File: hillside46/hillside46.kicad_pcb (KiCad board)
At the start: 2 copper layers, 142.5 x 99.9 mm, 80 parts, among them J1 Haptic, J2 TRRS, J3 Bat_Pos, J4 Bat_Neg, J5 Bat_Pos, J6 Bat_Neg, K1 SW_Key, K10 SW_Key, K11 SW_Key, K12 SW_Key, K13 SW_Key, K14 SW_Key, K15 SW_Key, K16 SW_Key, K17 SW_Key, K18 SW_Key, K19 SW_Rotary, K2 SW_Key, K23 SW_Rotary, K24 SW_Key, K25 SW_Key, K26 SW_Key, K3 SW_Key, K4 SW_Key, K5 SW_Key, K6 SW_Key, K7 SW_Key, K8 SW_Key, K9 SW_Key, SW1 Reset, SW2 SW_Power, U1 ProMicro_r

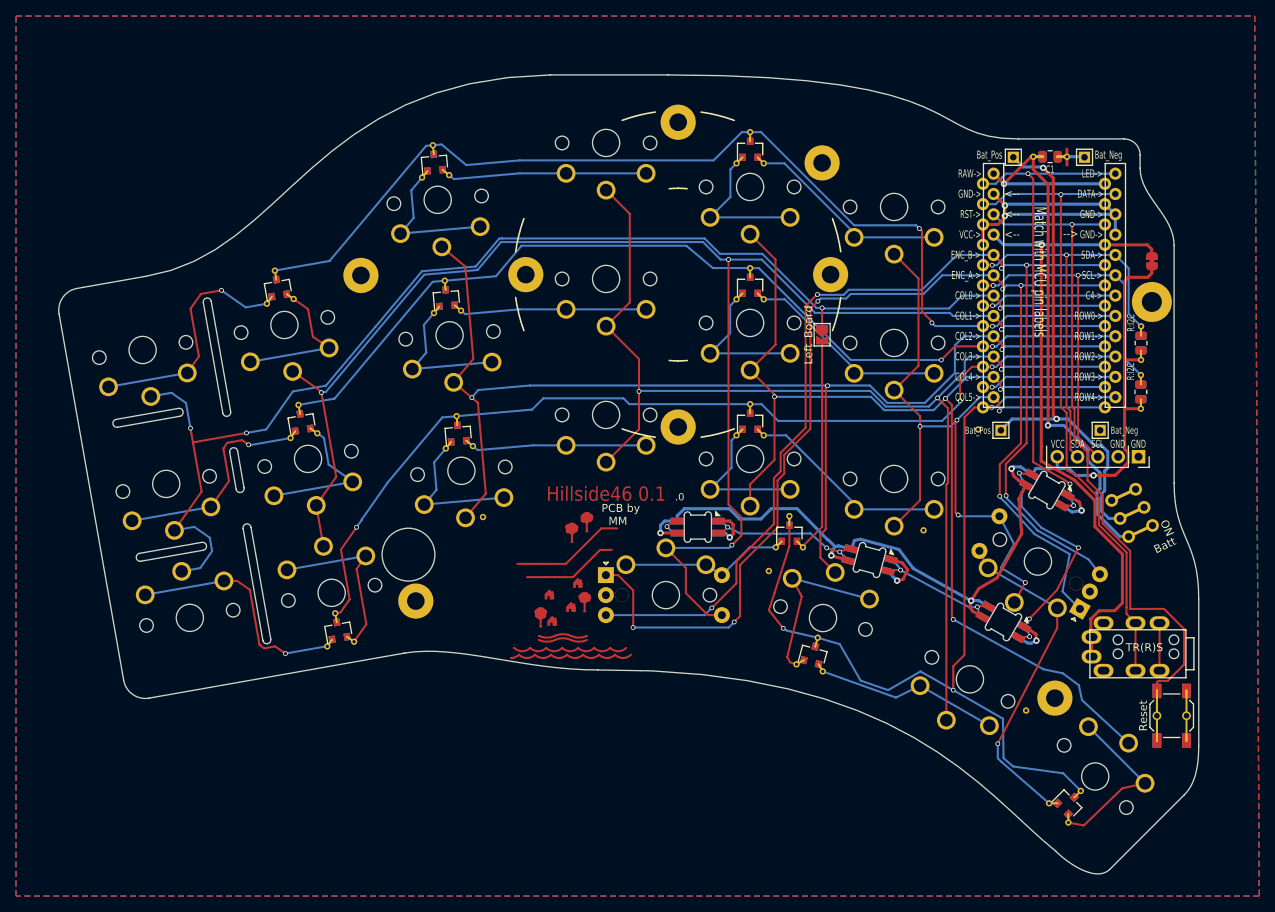
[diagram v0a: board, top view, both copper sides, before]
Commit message: 46: Fix bump-on spots and cutout callouts
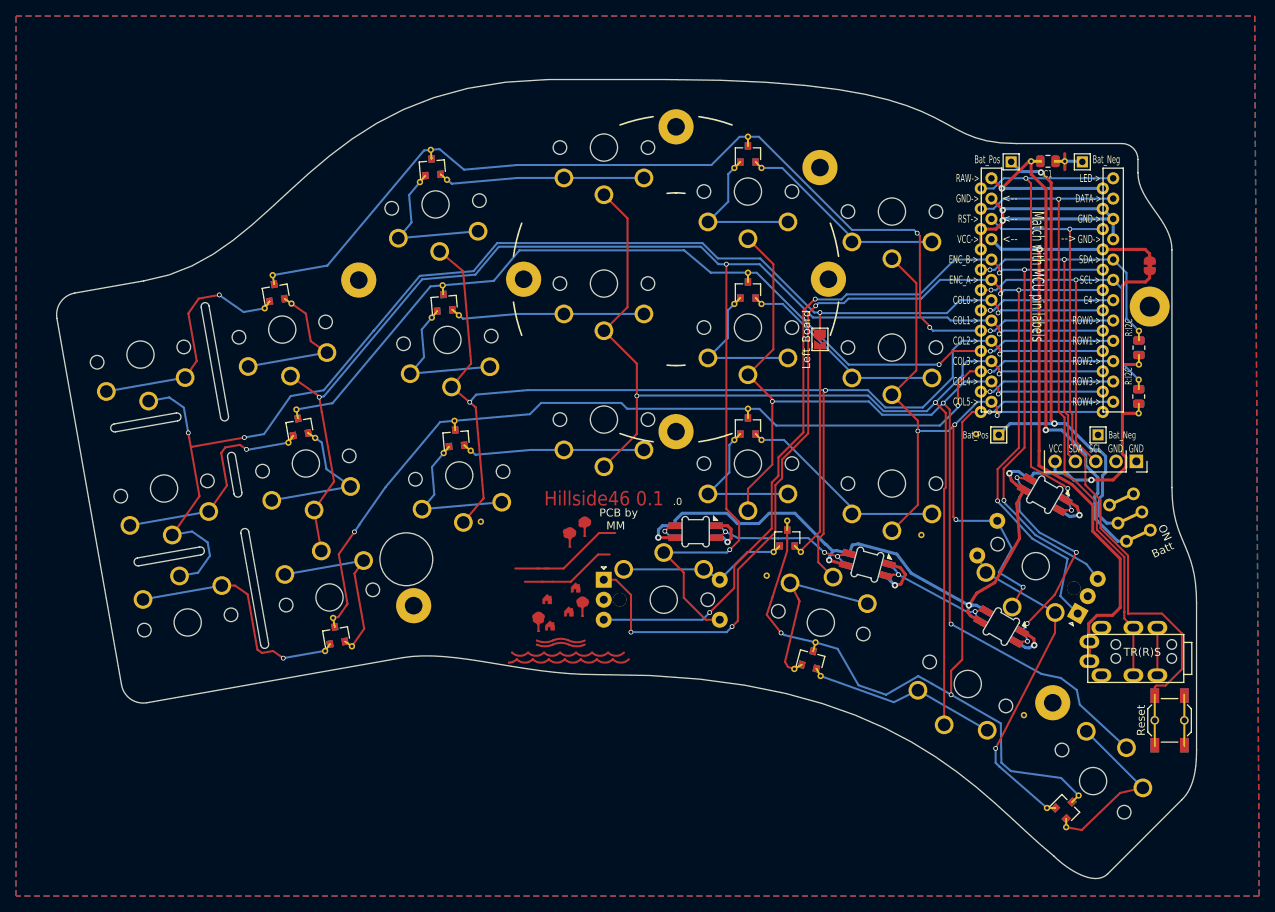
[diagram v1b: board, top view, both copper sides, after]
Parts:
- moved H17 119.6 mm to (185.2, 61.4), turned to 0 degrees
- moved H8 22.8 mm to (170.5, 124.4)
- moved H11 16.5 mm to (133.7, 120.5)
- moved H2 15.8 mm to (105.6, 123.3)
- moved H13 2.65 mm to (88.7, 99.5)
- moved H12 1.21 mm to (93.3, 126.0)
- moved D15 0.64 mm to (166.0, 96.0)
- moved H19 0.64 mm to (200.5, 137.1)
- moved K26 0.64 mm to (209.2, 140.4)
- moved C1 0.64 mm to (203.5, 62.9)
- moved D19 0.64 mm to (170.9, 110.0)
- moved D3 0.64 mm to (180.9, 113.3)
- moved D4 0.64 mm to (159.5, 109.2)
- moved D8 0.64 mm to (126.6, 63.6)
- moved H21 0.64 mm to (203.8, 68.8)
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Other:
- board text added: "CUT"

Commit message: 46: Cleanup edge, logo, row numbers
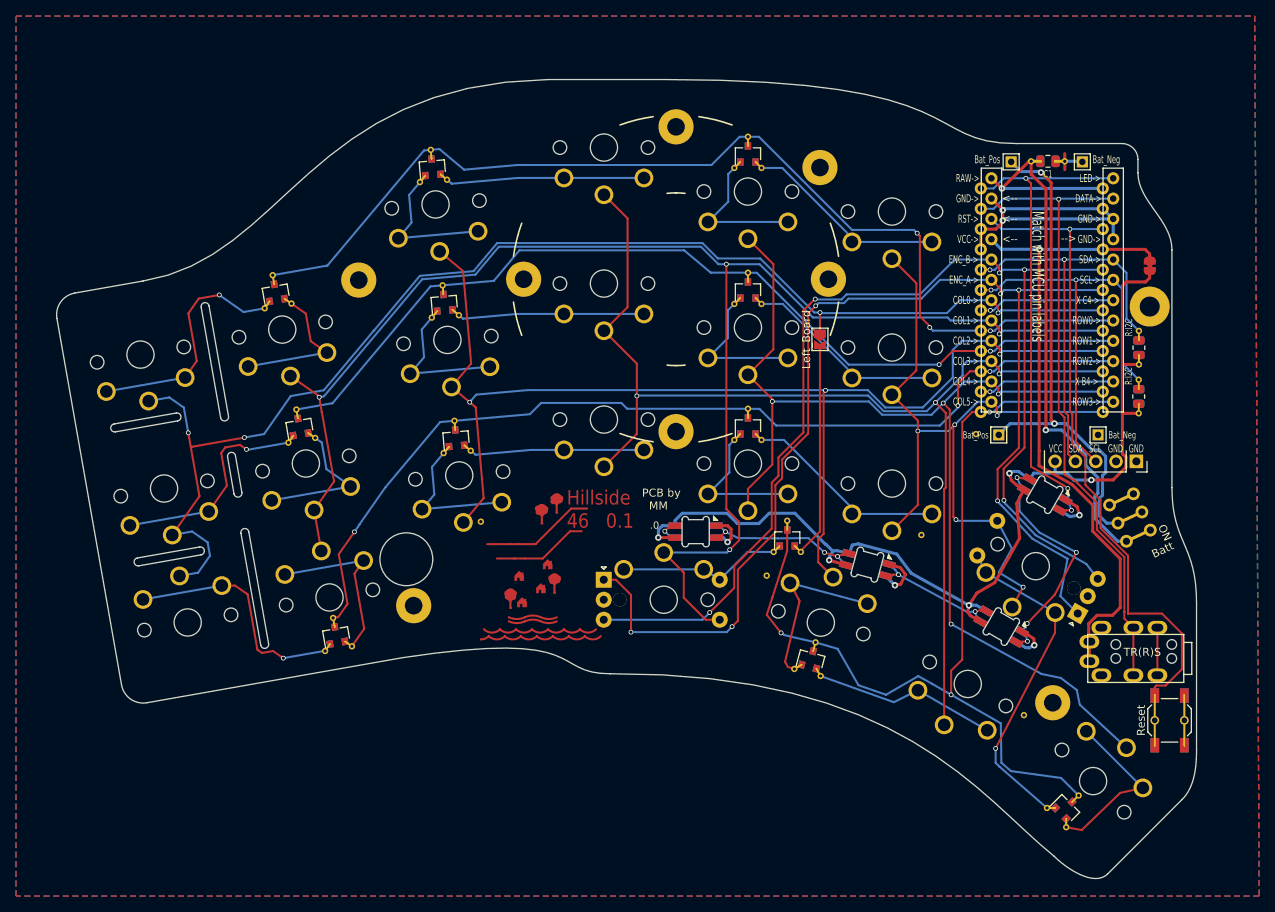
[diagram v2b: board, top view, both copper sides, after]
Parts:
- moved H3 4.55 mm to (139.6, 114.1)
- moved H11 2.55 mm to (135.6, 118.8)
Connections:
- net row4 renamed row3
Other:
- outline, holes or cut-outs redrawn
- board text added: "Hillside 46 0.1"
- board text removed: "Hillside46 0.1"

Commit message: 46: PCBA
- BOM JLC part numbers, type, and cost
- ESD protection chip
- PCBA Tooling holes
- Resistor values
- Reset switch model
- BOM excludes switches, vias, etch
- Paste layers
- JLC order number silk
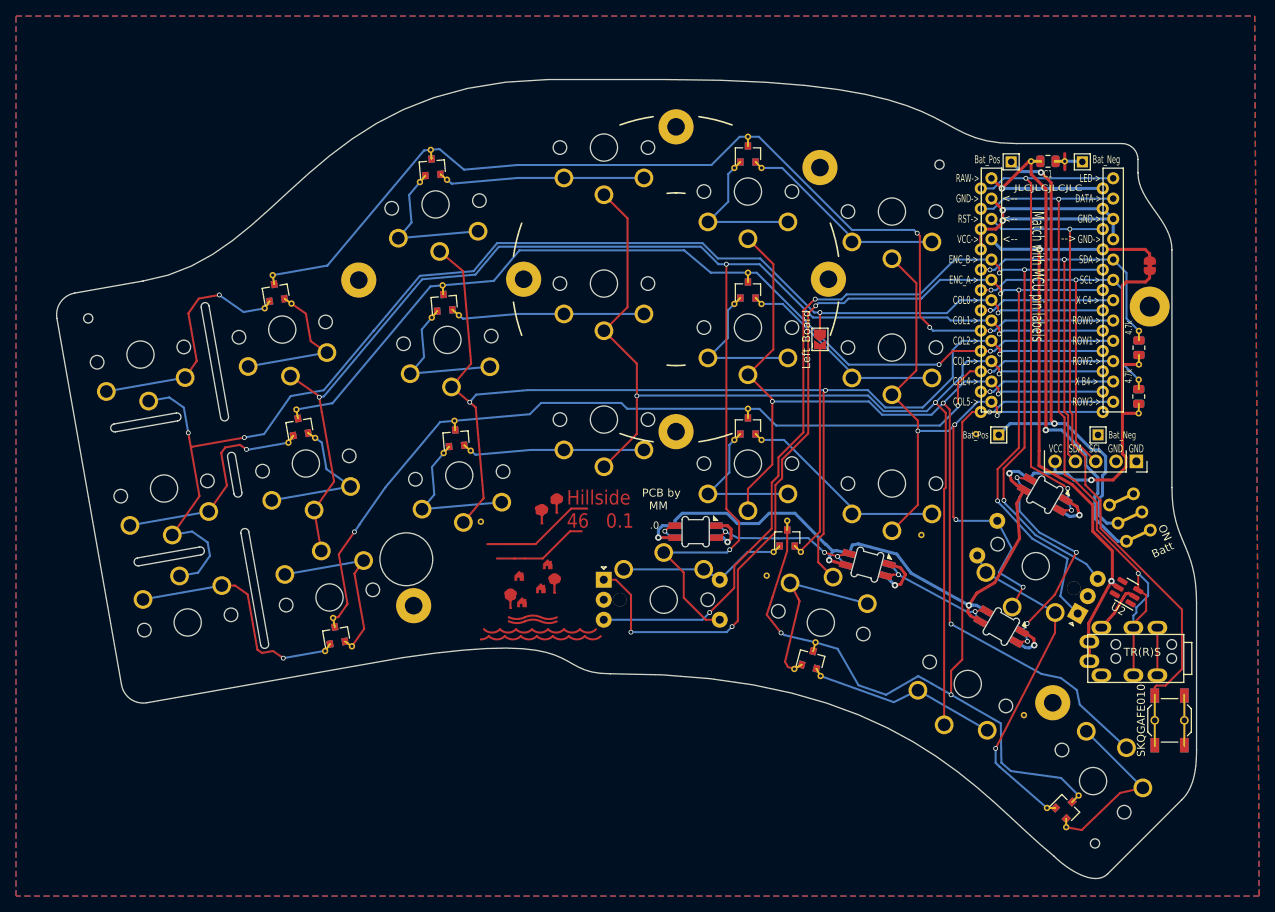
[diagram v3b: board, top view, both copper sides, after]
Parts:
- added H23: ToolingHole, hillside_basic:ToolingHole_1.152mm, F.Cu at (190.0, 63.3)
- added H24: ToolingHole, hillside_basic:ToolingHole_1.152mm, F.Cu at (83.6, 82.5)
- added H25: ToolingHole, hillside_basic:ToolingHole_1.152mm, F.Cu at (209.4, 148.2)
- added U2: SRV05-4, Package_TO_SOT_SMD:SOT-23-6, F.Cu at (213.3, 116.7)
- R1, R2: value R:I2C -> 4.7k
- SW1: value Reset -> SKQGAFE010
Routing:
- net data: track 80.7 -> 90.3 mm, vias 1 -> 2
- net GND: track 66.8 -> 73.2 mm
- net reset: track 83.1 -> 80.6 mm
- net VCC: track 80.6 -> 80.4 mm, vias 1 -> 2
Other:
- board text added: "JLCJLCJLCJLC"

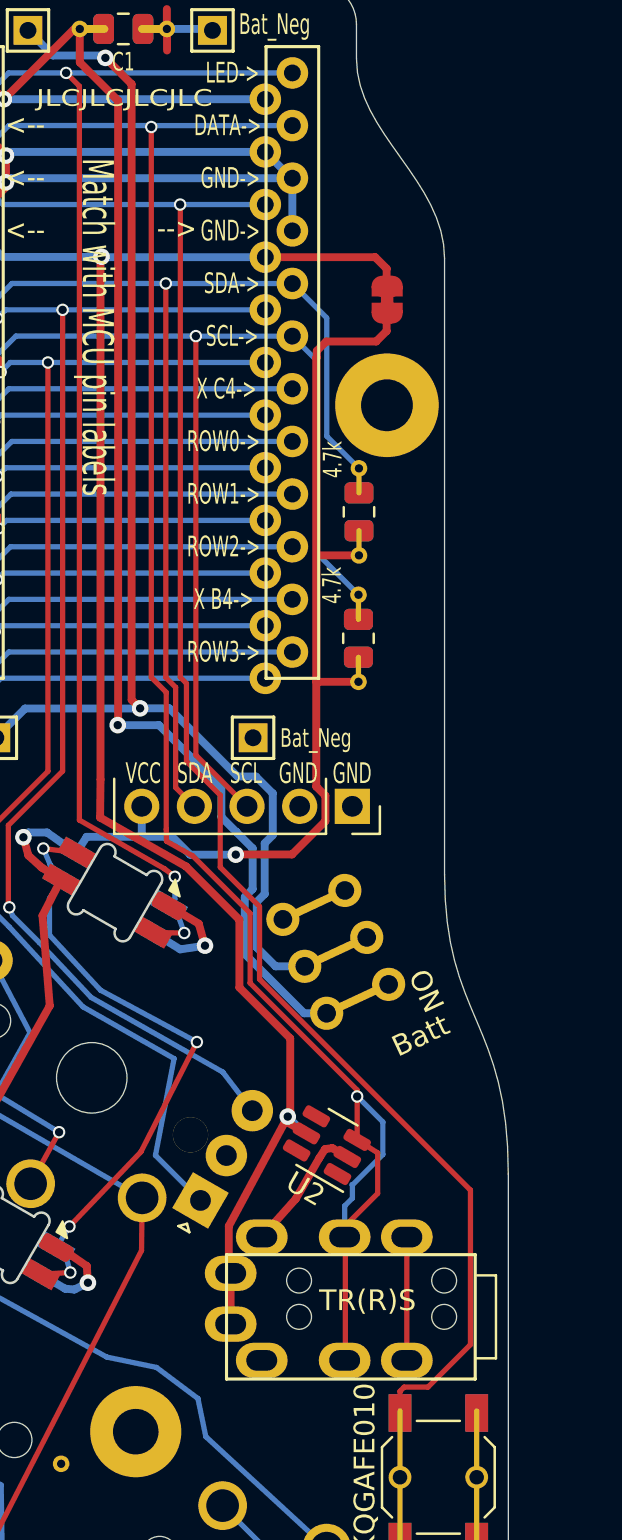
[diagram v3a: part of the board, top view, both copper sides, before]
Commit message: 46: Add prices, renumber keys, LCSC Part #
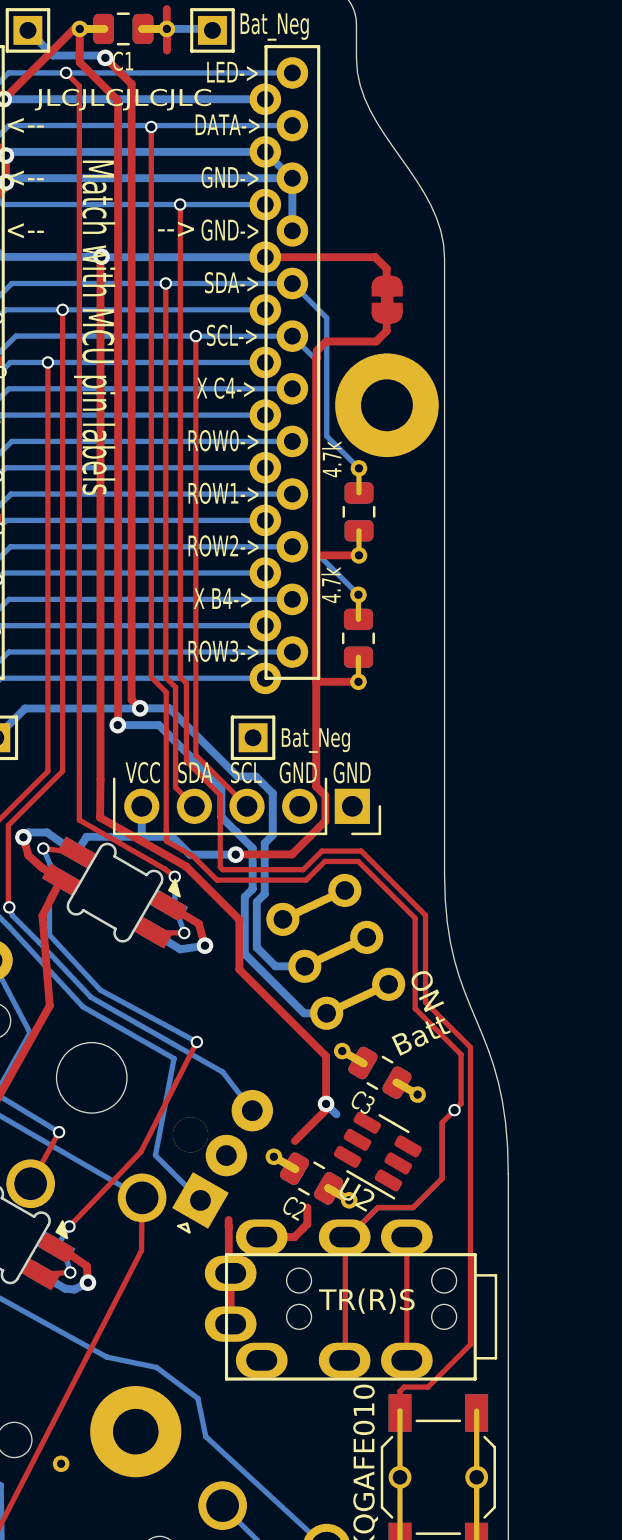
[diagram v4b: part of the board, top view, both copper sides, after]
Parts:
- added C2: 4u7, hillside_basic:C_0805_2012Metric, F.Cu at (212.6, 118.4)
- added C3: 4u7, hillside_basic:C_0805_2012Metric, F.Cu at (215.9, 113.3)
- moved U2 2.48 mm to (215.8, 117.1)
- renumbered K23 to K20, K24 to K21, K25 to K22, K26 to K23
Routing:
- net data: track 90.3 -> 100.1 mm
- net reset: track 80.6 -> 85.8 mm
- net VCC: track 80.4 -> 75.7 mm
- net GND: track 73.2 -> 70.0 mm
